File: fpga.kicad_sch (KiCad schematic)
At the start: 52 parts, among them Q1 BSS138PW, SW1 SW_B3U-1000P_SMD, U1 ICE40UP5K-SG48, U2 W25Q32JW_SOIC-8

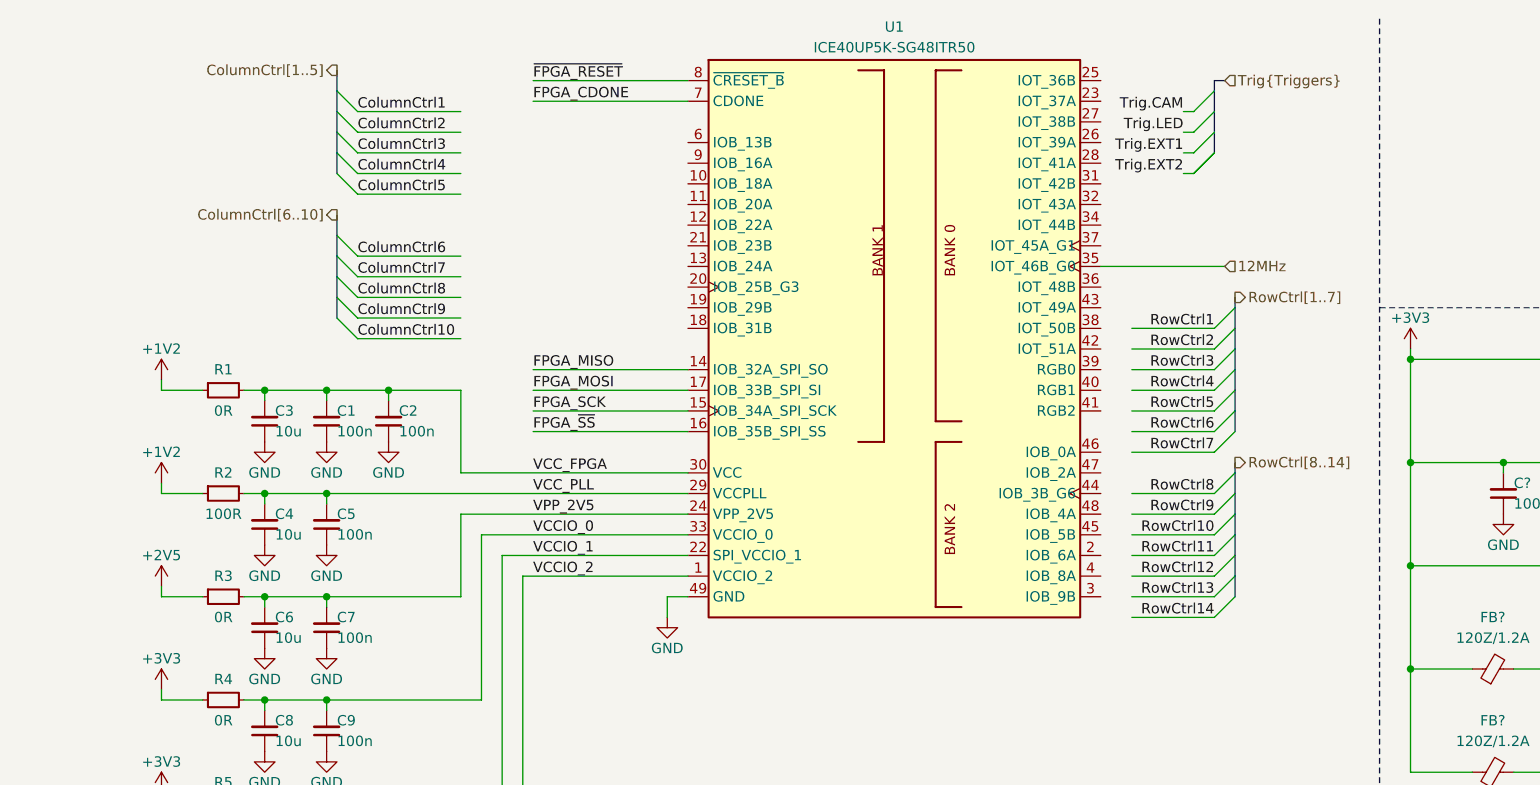
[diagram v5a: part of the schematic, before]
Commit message: [#72133] Coonect matrix control signals to uC/FPGA
Signed-off-by: Dawid Lentka <dlentka@antmicro.com>
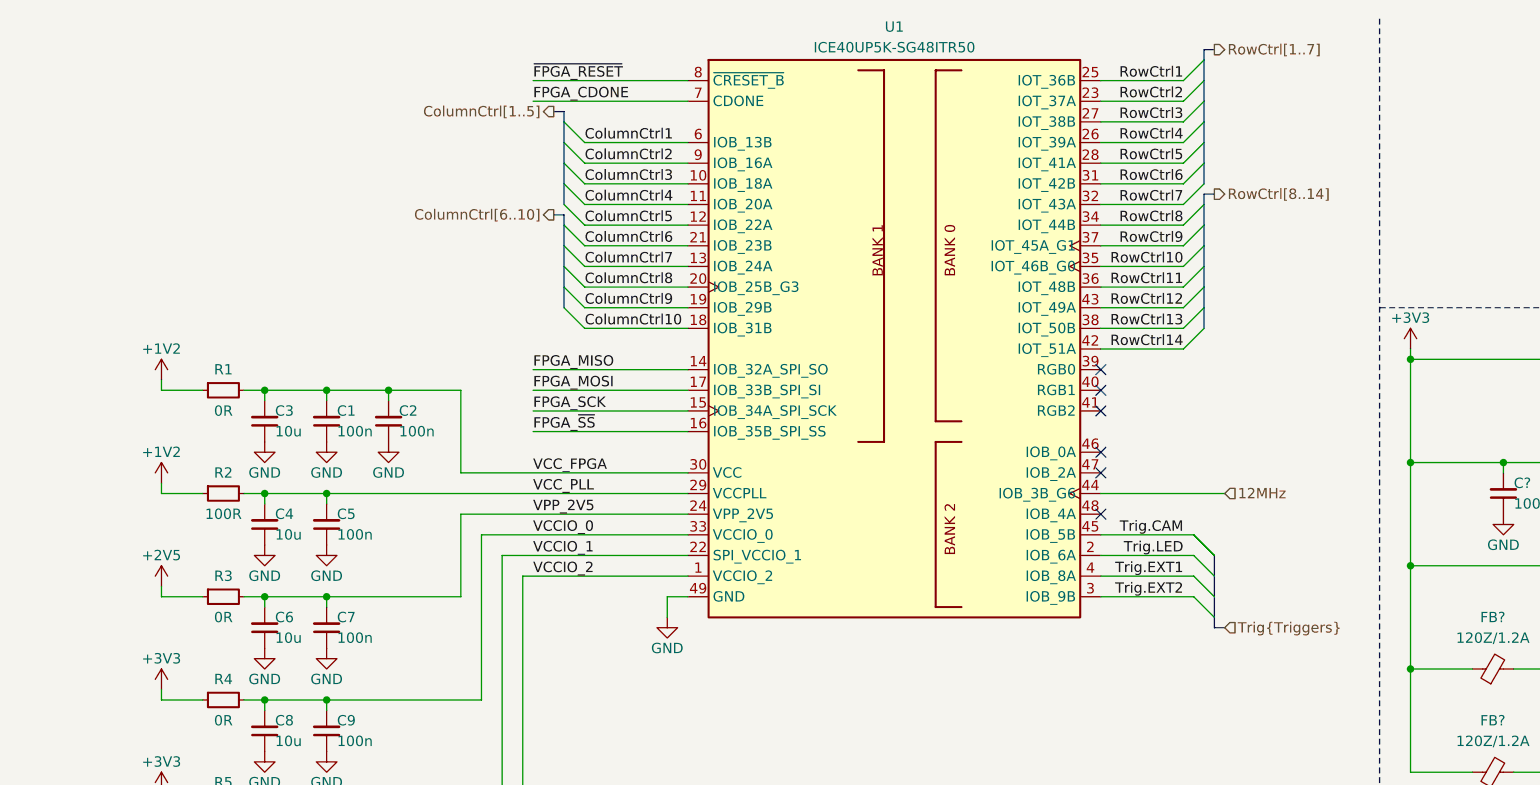
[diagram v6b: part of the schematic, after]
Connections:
- net 12MHz: now also U1.44 (IOB_3B_G6); no longer U1.35 (IOT_46B_G0)
- net ColumnCtrl1: now also U1.6 (IOB_13B)
- net ColumnCtrl10: now also U1.18 (IOB_31B)
- net ColumnCtrl2: now also U1.9 (IOB_16A)
- net ColumnCtrl3: now also U1.10 (IOB_18A)
- net ColumnCtrl4: now also U1.11 (IOB_20A)
- net ColumnCtrl5: now also U1.12 (IOB_22A)
- net ColumnCtrl6: now also U1.21 (IOB_23B)
- net ColumnCtrl7: now also U1.13 (IOB_24A)
- net ColumnCtrl8: now also U1.20 (IOB_25B_G3)
- net ColumnCtrl9: now also U1.19 (IOB_29B)
- net RowCtrl1: now also U1.25 (IOT_36B)
- net RowCtrl10: now also U1.35 (IOT_46B_G0)
- net RowCtrl11: now also U1.36 (IOT_48B)
- net RowCtrl12: now also U1.43 (IOT_49A)
- net RowCtrl13: now also U1.38 (IOT_50B)
- net RowCtrl14: now also U1.42 (IOT_51A)
- net RowCtrl2: now also U1.23 (IOT_37A)
- net RowCtrl3: now also U1.27 (IOT_38B)
- net RowCtrl4: now also U1.26 (IOT_39A)
- net RowCtrl5: now also U1.28 (IOT_41A)
- net RowCtrl6: now also U1.31 (IOT_42B)
- net RowCtrl7: now also U1.32 (IOT_43A)
- net RowCtrl8: now also U1.34 (IOT_44B)
- net RowCtrl9: now also U1.37 (IOT_45A_G1)
- net Trig.CAM: now also U1.45 (IOB_5B)
- net Trig.EXT1: now also U1.4 (IOB_8A)
- net Trig.EXT2: now also U1.3 (IOB_9B)
- net Trig.LED: now also U1.2 (IOB_6A)
- no-connect marks 17 -> 23

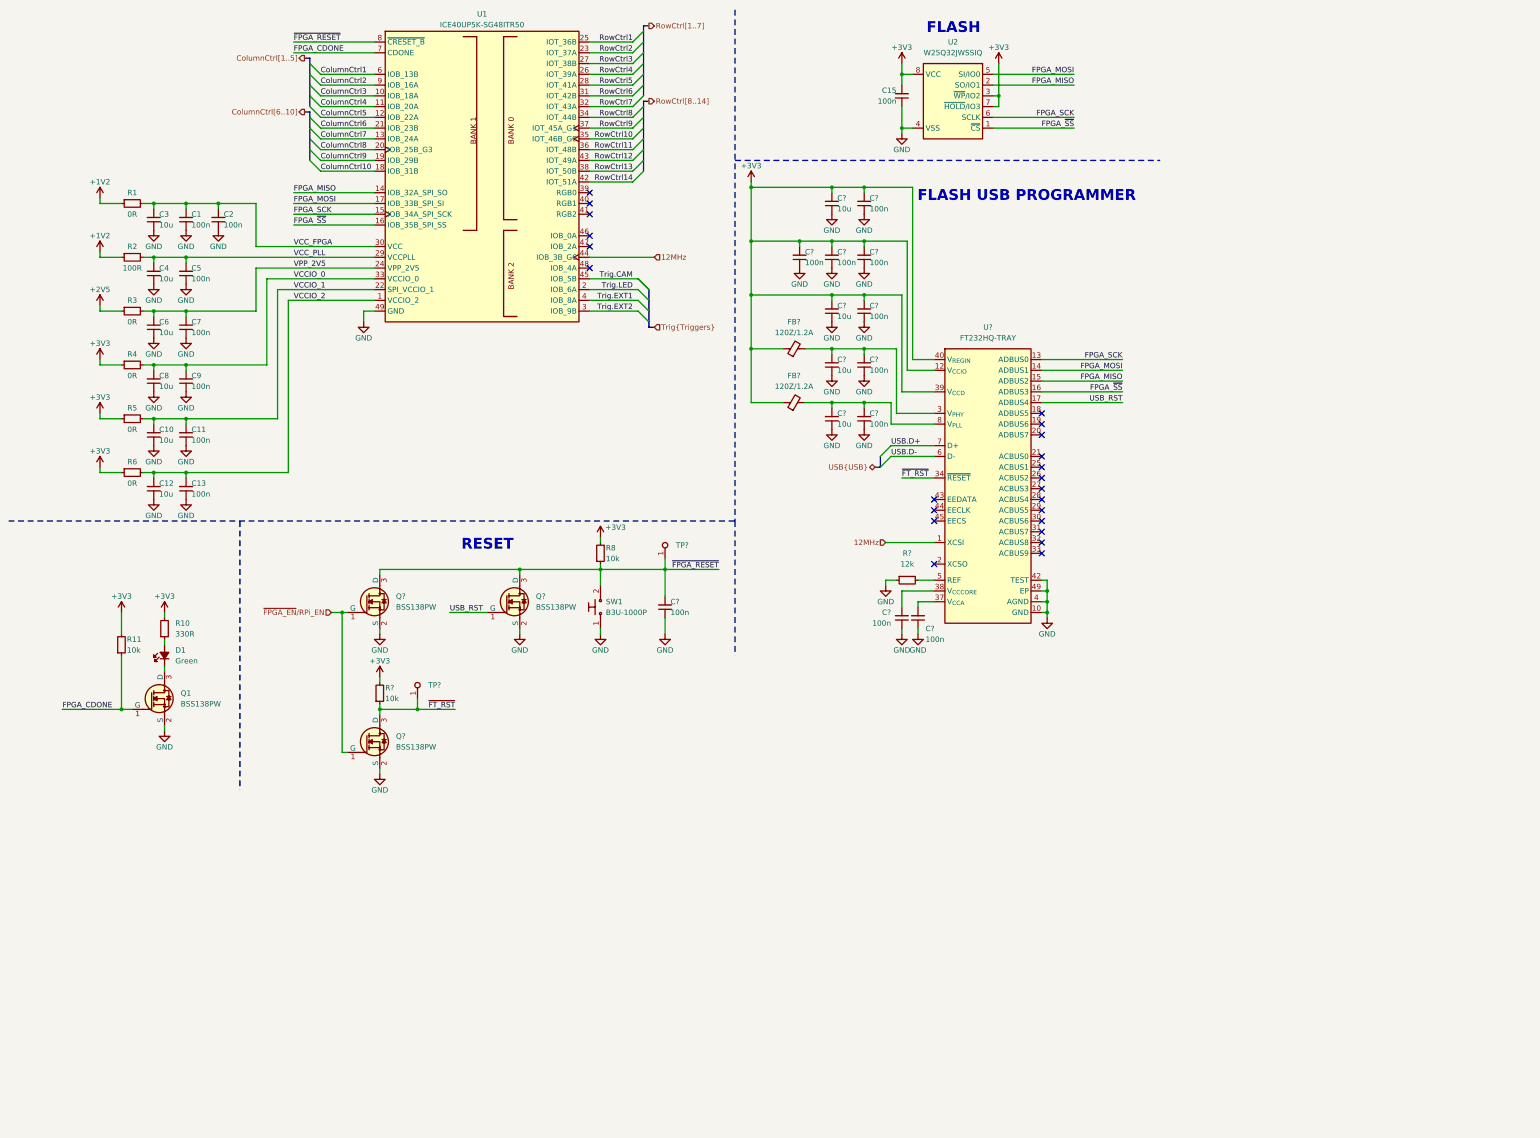
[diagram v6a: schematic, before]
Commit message: [#72133] Annotate schematics
Signed-off-by: Dawid Lentka <dlentka@antmicro.com>
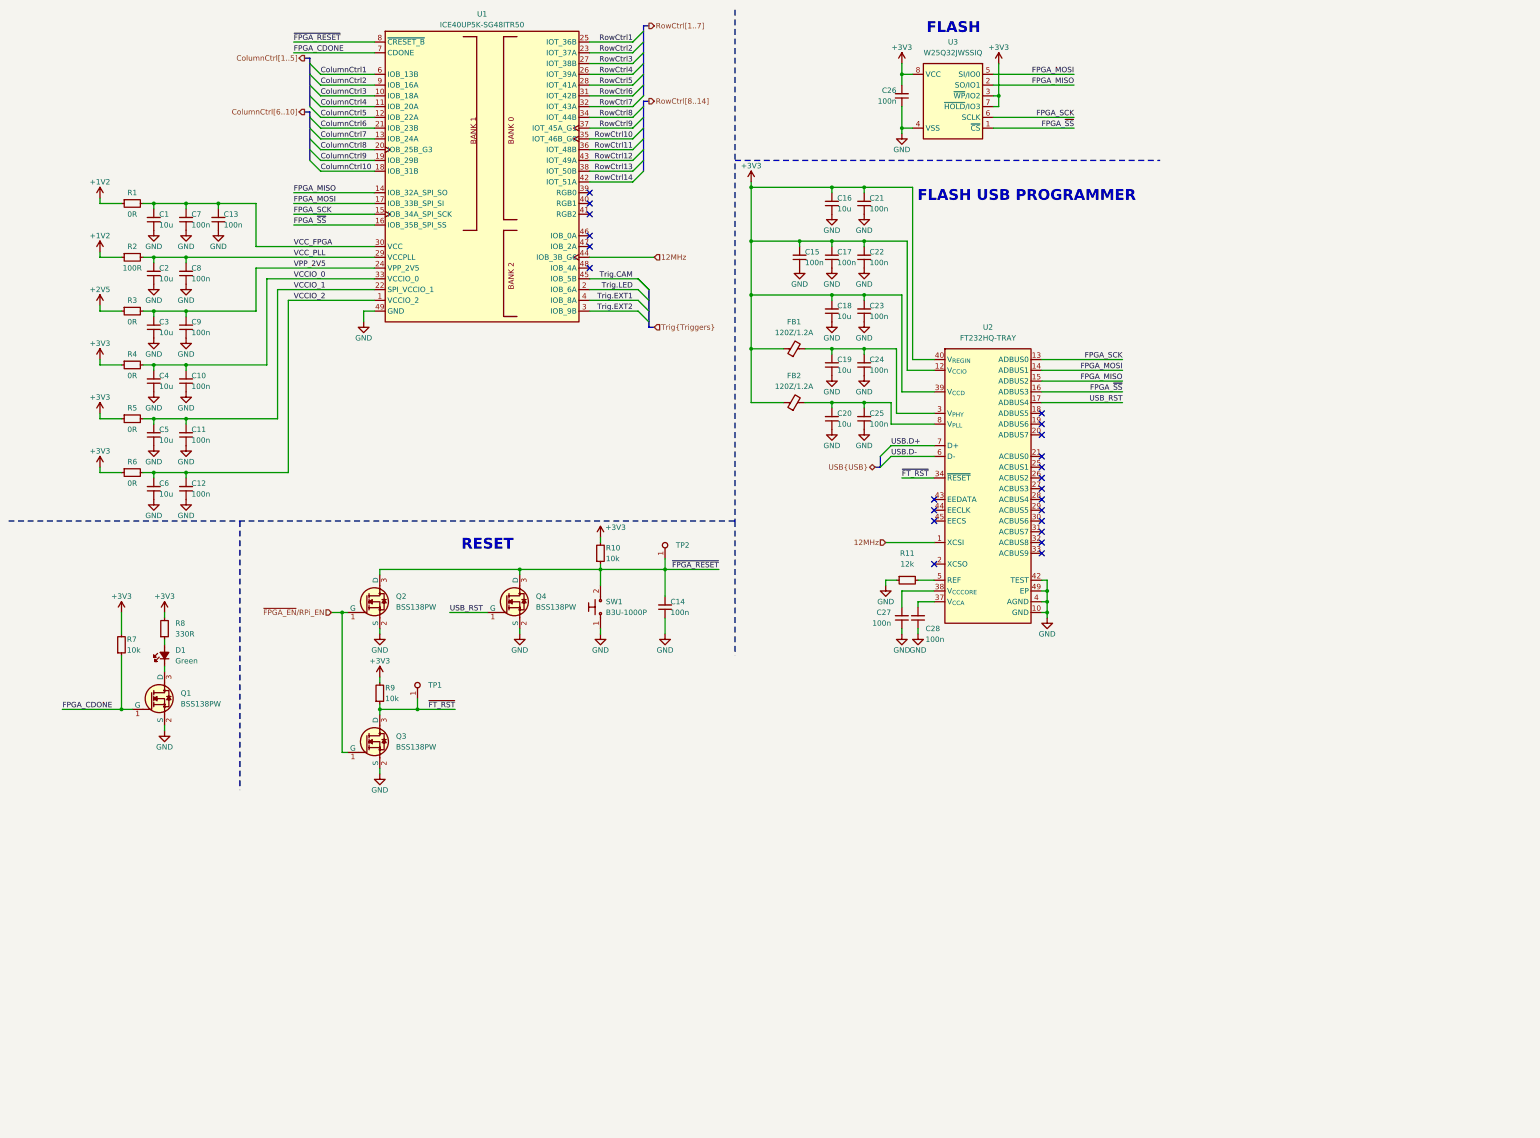
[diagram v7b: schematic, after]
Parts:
- gave numbers to parts that had none: 24
- renumbered C3 to C1, C9 to C10, C13 to C12, C2 to C13, C4 to C2, C15 to C26, C6 to C3, C8 to C4, C10 to C5, C12 to C6, C1 to C7, C5 to C8, C7 to C9, R8 to R10, R11 to R7, R10 to R8, U2 to U3

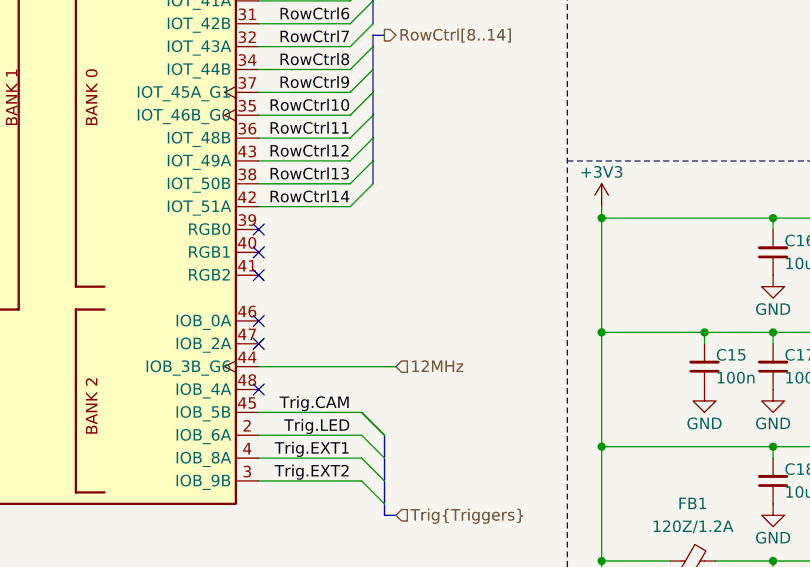
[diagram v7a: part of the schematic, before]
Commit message: [#72133] Sch: Add IMU
Signed-off-by: Dawid Lentka <dlentka@antmicro.com>
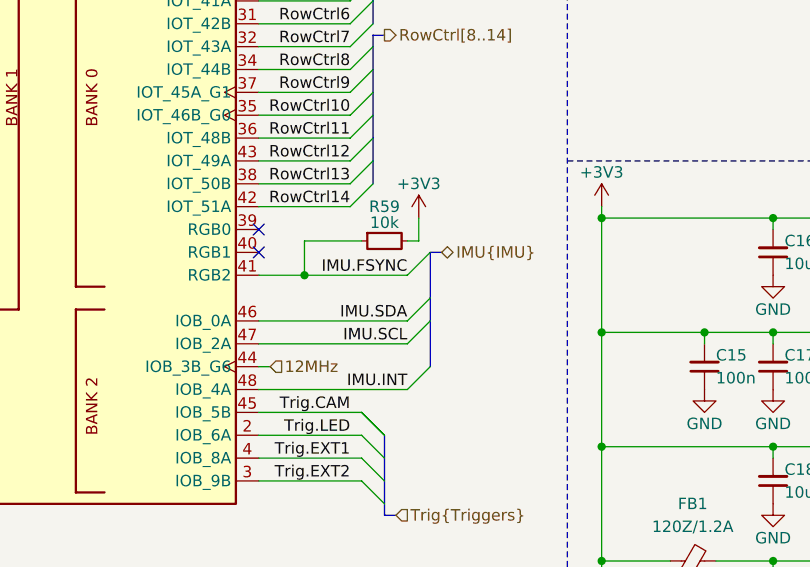
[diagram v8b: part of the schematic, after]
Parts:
- added R59: R_10k_0402, antmicro-footprints:R_0402_1005Metric, symbol antmicroResistors0402:R_10k_0402
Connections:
- net +3V3: now also R59.2
- net IMU.FSYNC: now reaches U1.41 (RGB2)
- net IMU.FSYNC: now also R59.1
- net IMU.SDA: now reaches U1.46 (IOB_0A)
- net IMU.SCL: now reaches U1.47 (IOB_2A)
- net IMU.INT: now reaches U1.48 (IOB_4A)
- no-connect marks 23 -> 19
